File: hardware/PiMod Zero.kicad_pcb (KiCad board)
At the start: 2 copper layers, 65 x 30 mm, 47 parts, among them J1 RPi_GPIO, J2 Pi Video, J3 Amphenol 531-40101, SW1 SW_SPDT, U1 NJM2519A, X1 F88SM

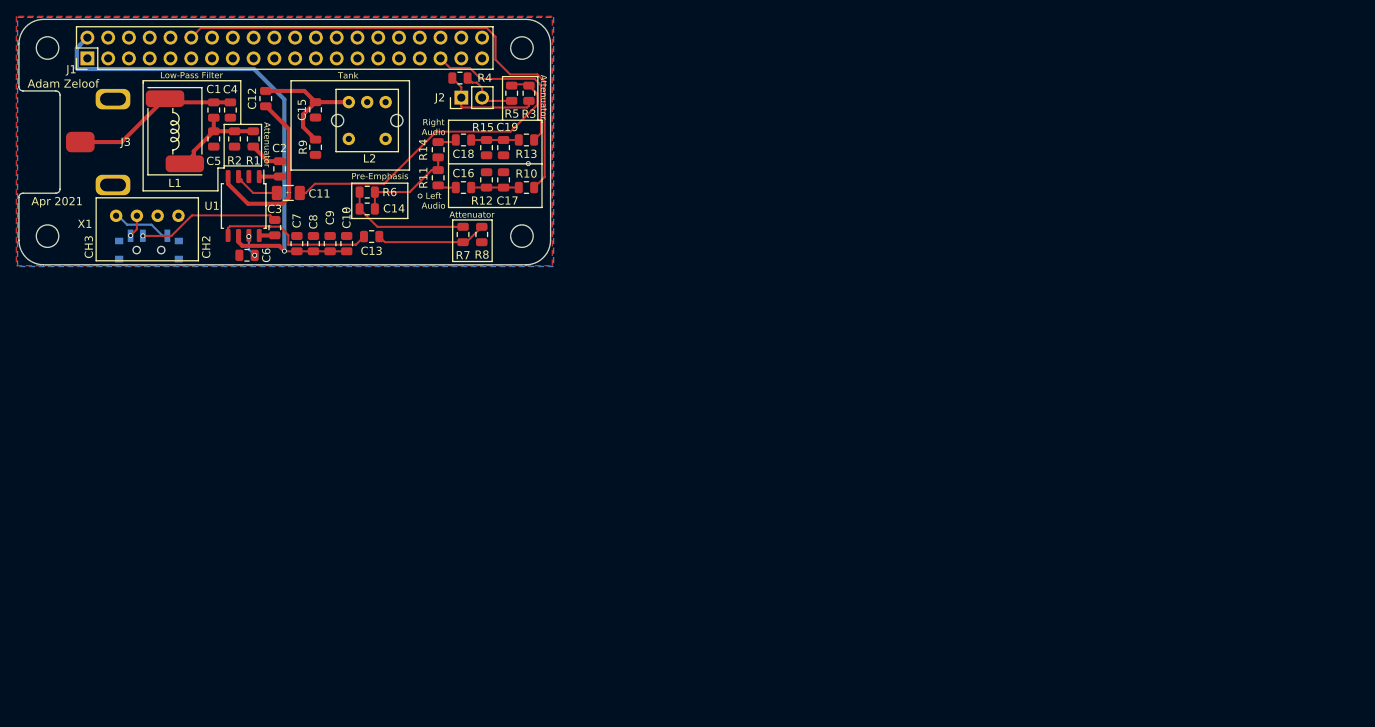
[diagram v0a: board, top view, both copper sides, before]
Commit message: Updated 3D models
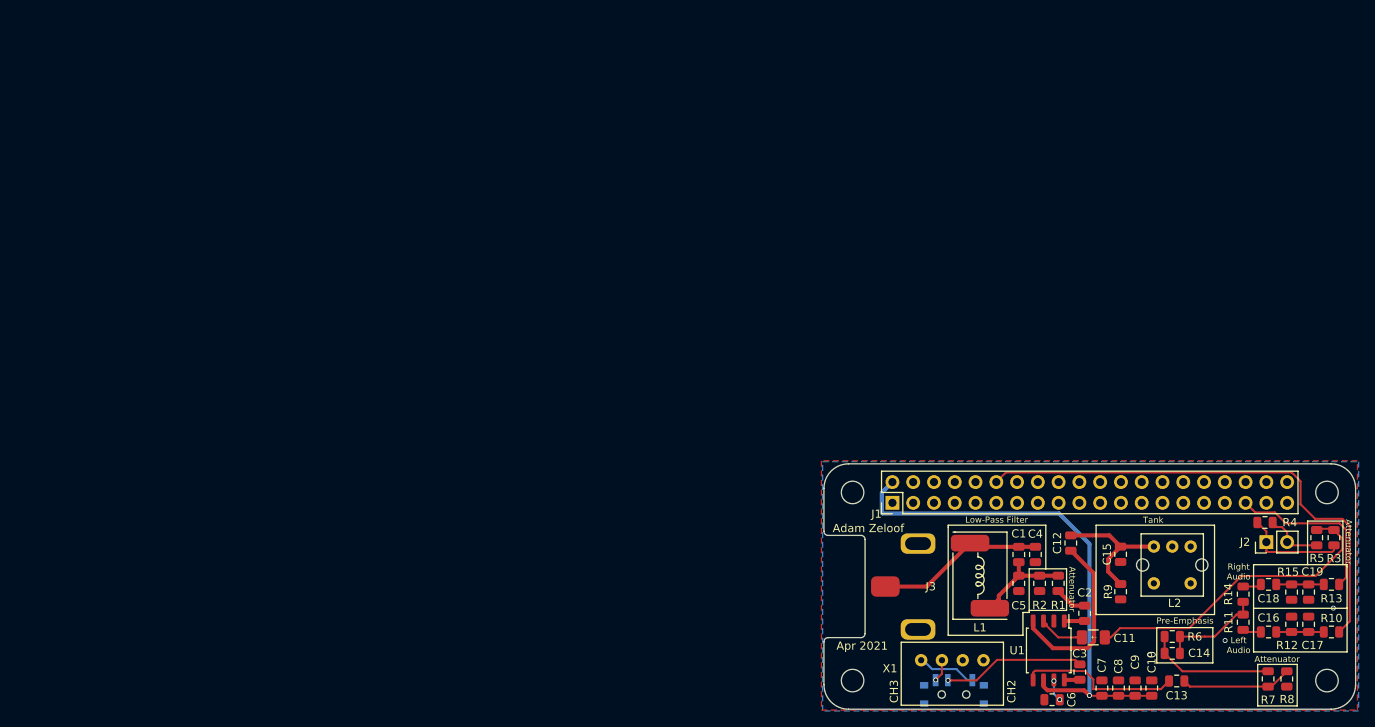
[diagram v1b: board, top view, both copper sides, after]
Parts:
- L2: footprint rf_modulator:Coilcraft Slot 7 Inductor -> rf_modulator:Coilcraft-Slot-7-Inductor
- moved ? 112.4 mm to (114.4, 105.3)
- moved ? 112.4 mm to (172.4, 82.3)
- moved ? 112.4 mm to (172.4, 105.3)
- moved ? 112.4 mm to (114.4, 82.3)
- moved C1 112.4 mm to (134.7, 89.9)
- moved C11 112.4 mm to (143.9, 100.1)
- moved C12 112.4 mm to (141.1, 88.5)
- moved C14 112.4 mm to (153.5, 102.0)
- moved C15 112.4 mm to (147.2, 89.9)
- moved C16 112.4 mm to (165.3, 99.4)
- moved C17 112.4 mm to (170.2, 98.5)
- moved C18 112.4 mm to (165.3, 93.6)
- moved C19 112.4 mm to (170.2, 94.5)
- moved C5 112.4 mm to (134.7, 93.5)
- moved C6 112.4 mm to (138.8, 107.7)
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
